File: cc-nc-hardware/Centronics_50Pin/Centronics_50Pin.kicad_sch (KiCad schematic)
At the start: 85 parts, among them J1 Conn_01x03_Male, J4 SW, J6 Conn_01x02_Male, SW1 SW_MEC_5E, U1 SN74CBTD3384, U10 Centronics50PinMale, U2 SN74CBTD3384, U3 AMS1117-2.85, U4 LVT245, U5 LVT125, U6 LVT125, U7 LVT125, U9 LVT245

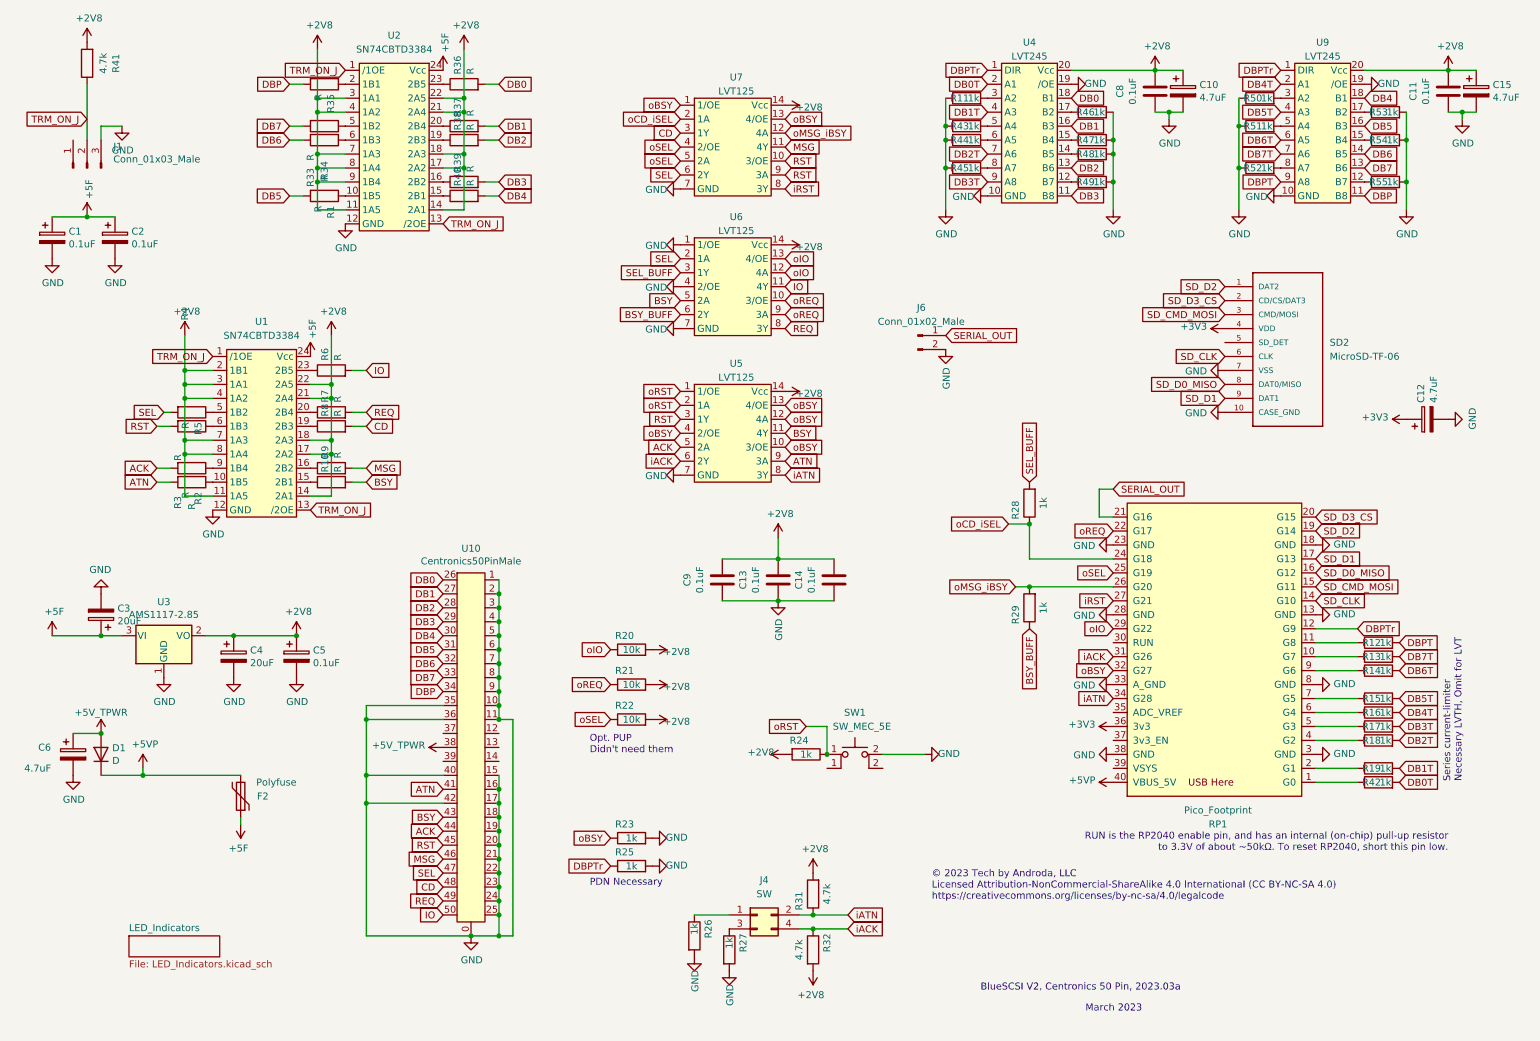
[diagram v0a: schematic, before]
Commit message: New version of C50, shorter and with options for voltage regulator
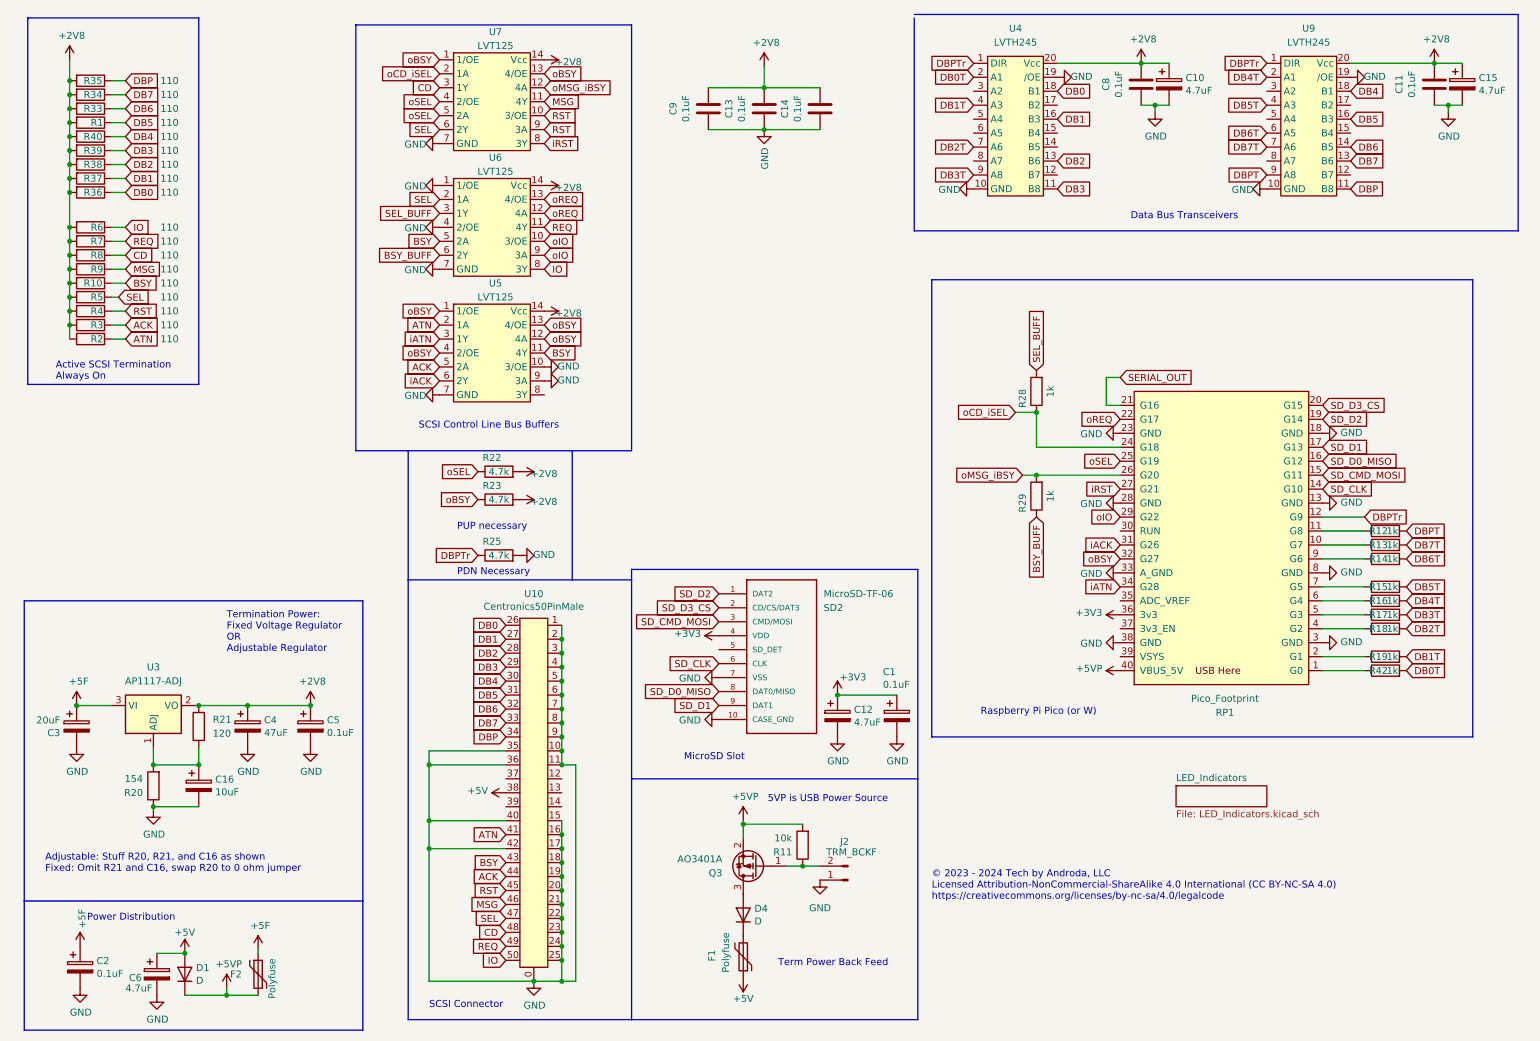
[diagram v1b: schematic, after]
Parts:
- removed J1: Conn_01x03_Male, Connector_PinHeader_2.54mm:PinHeader_1x03_P2.54mm_Vertical, symbol Connector:Conn_01x03_Male
- removed J4: SW, Connector_PinHeader_2.54mm:PinHeader_2x02_P2.54mm_Vertical, symbol Connector_Generic:Conn_02x02_Odd_Even
- removed J6: Conn_01x02_Male, Connector_PinHeader_2.54mm:PinHeader_1x02_P2.54mm_Vertical, symbol Connector:Conn_01x02_Male
- removed R24, R26, R27: 1k, Resistor_SMD:R_0603_1608Metric_Pad0.98x0.95mm_HandSolder, symbol Device:R
- removed R31, R32, R41: 4.7k, Resistor_SMD:R_0603_1608Metric_Pad0.98x0.95mm_HandSolder, symbol Device:R
- removed R43, R44, R45, R46, R47, R48, R49, R50, R51, R52, R53, R54, R55: 1k, Resistor_SMD:R_0402_1005Metric_Pad0.72x0.64mm_HandSolder, symbol Device:R
- removed SW1: SW_MEC_5E, Library:TS-1187A-B-A-B, symbol Switch:SW_MEC_5E
- removed U1, U2: SN74CBTD3384, Package_SO:TSSOP-24_4.4x7.8mm_P0.65mm, symbol New_Library:SN74CBTD3384
- removed U3: AMS1117-2.85, Package_TO_SOT_SMD:SOT-223-3_TabPin2, symbol Regulator_Linear:AMS1117CD-2.85
- added C16: 10uF, Capacitor_SMD:C_0603_1608Metric, symbol Device:CP
- added D4: D, Diode_SMD:D_SMA, symbol Device:D
- added F1: Polyfuse, Fuse:Fuse_0805_2012Metric_Pad1.15x1.40mm_HandSolder, symbol Device:Polyfuse
- added J2: TRM_BCKF, Connector_PinHeader_2.54mm:PinHeader_1x02_P2.54mm_Vertical, symbol Connector:Conn_01x02_Pin
- added Q3: AO3401A, Package_TO_SOT_SMD:SOT-23, symbol Transistor_FET:AO3401A
- added U3: AP1117-ADJ, Package_TO_SOT_SMD:SOT-223-3_TabPin2, symbol Regulator_Linear:AP1117-ADJ
- C1, C12, C2, C5, C6: footprint Capacitor_SMD:C_0805_2012Metric_Pad1.15x1.40mm_HandSolder -> Capacitor_SMD:C_0603_1608Metric
- C10, C11, C13, C14, C15, C8, C9: footprint Capacitor_SMD:C_0805_2012Metric_Pad1.18x1.45mm_HandSolder -> Capacitor_SMD:C_0603_1608Metric
- C4: value 20uF -> 47uF
- R1, R10, R2, R3, R33, R34, R35, R36, R37, R38, R39, R4, R40, R5, R6, R7, R8, R9: value R -> 110
- R11: value 1k -> 10k; footprint Resistor_SMD:R_0402_1005Metric_Pad0.72x0.64mm_HandSolder -> Resistor_SMD:R_0603_1608Metric
- R20: value 10k -> 154; footprint Resistor_SMD:R_0603_1608Metric_Pad0.98x0.95mm_HandSolder -> Resistor_SMD:R_0603_1608Metric
- R21: value 10k -> 120; footprint Resistor_SMD:R_0603_1608Metric_Pad0.98x0.95mm_HandSolder -> Resistor_SMD:R_0805_2012Metric
- R22: value 10k -> 4.7k
- R23, R25: value 1k -> 4.7k
- U4, U9: value LVT245 -> LVTH245
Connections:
- net +2V8: now also R1.2, R10.2, R2.2, R23.2, R3.2, R33.2, R34.2, R35.2, R36.2, R37.2, R38.2, R39.2, R4.2, R40.2, R5.2, R6.2, R7.2, R8.2, R9.2, U3.2 (VO); no longer R20.2
- net +3V3: now also C1.1
- net +5F: now also U3.3 (VI); no longer C1.1
- net +5V: now also F1.1
- net +5VP: now also R11.2, Q3.2 (S)
- net ACK: now also R3.1; no longer R3.2
- net ATN: now also R2.1, U5.2 (1A); no longer R2.2, U5.9 (3A)
- net BSY: now also R10.1; no longer R10.2
- net CD: now also R8.1; no longer R8.2
- net DB0: now also R36.1; no longer R36.2
- net DB1: now also R37.1; no longer R37.2
- net DB2: now also R38.1; no longer R38.2
- net DB3: now also R39.1; no longer R39.2
- net DB4: now also R40.1; no longer R40.2
- net DB5: now also R1.1; no longer R1.2
- net DB6: now also R33.1; no longer R33.2
- net DB7: now also R34.1; no longer R34.2
- net DBP: now also R35.1; no longer R35.2
- net GND: now also R20.1, U5.10 (3/OE), U5.9 (3A), C16.2, J2.1 (Pin_1); no longer R11.1, R23.2
- net IO: now also R6.1, U6.8 (3Y); no longer R6.2, U6.11 (4Y)
- net MSG: now also R9.1; no longer R9.2
- net REQ: now also R7.1, U6.11 (4Y); no longer R7.2, U6.8 (3Y)
- net RST: now also R4.1; no longer R4.2, U5.3 (1Y)
- net SEL: now also R5.1; no longer R5.2
- net iATN: now also U5.3 (1Y); no longer U5.8 (3Y)
- net oBSY: now also U5.1 (1/OE); no longer U5.10 (3/OE)
- net oIO: now also U6.10 (3/OE), U6.9 (3A); no longer R20.1, U6.12 (4A), U6.13 (4/OE)
- net oREQ: now also U6.12 (4A), U6.13 (4/OE); no longer R21.1, U6.10 (3/OE), U6.9 (3A)
- net at U4.3 (A2): no longer R11.2
- removed net oRST: U5.1 (1/OE), U5.2 (1A)
- new net: C16.1, R20.2, R21.1, U3.1 (ADJ)
- new net: J2.2 (Pin_2), Q3.1 (G), R11.1
- new net: D4.2 (A), Q3.3 (D)
- new net: D4.1 (K), F1.2
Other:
- note added: "5VP is USB Power Source"
- note added: "Active SCSI Termination Always On"
- note added: "Adjustable: Stuff R20, R21, and C16 as shown Fixed: Omit R21 and C16, swap R20 to 0 ohm jumper"
- note added: "Data Bus Transceivers"
- note added: "MicroSD Slot"
- note added: "PUP necessary"
- note added: "Power Distribution"
- note added: "Raspberry Pi Pico (or W)"
- note added: "SCSI Connector"
- note added: "SCSI Control Line Bus Buffers"
- note added: "Term Power Back Feed"
- note added: "Termination Power: Fixed Voltage Regulator OR Adjustable Regulator"
- note added: "© 2023 - 2024 Tech by Androda, LLC Licensed Attribution-NonCommercial-ShareAlike 4.0 International (CC BY-NC-SA 4.0) https://creativecommons.org/licenses/by-nc-sa/4.0/legalcode"
- note removed: "BlueSCSI V2, Centronics 50 Pin, 2023.03a"
- note removed: "March 2023"
- note removed: "Opt. PUP Didn't need them"
- note removed: "RUN is the RP2040 enable pin, and has an internal (on-chip) pull-up resistor to 3.3V of about ~50kΩ. To reset RP2040, short this pin low."
- note removed: "Series current-limiter Necessary LVTH, Omit for LVT"
- note removed: "© 2023 Tech by Androda, LLC Licensed Attribution-NonCommercial-ShareAlike 4.0 International (CC BY-NC-SA 4.0) https://creativecommons.org/licenses/by-nc-sa/4.0/legalcode"
- company: (none) -> Tech by Androda, LLC
- title: (none) -> BlueSCSI V2, Centronics 50 Pin, 2024.03a
- moved on the sheet: C10, C11, C12, C13, C14, C15, C2, C3, C4, C5, C6, C8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
